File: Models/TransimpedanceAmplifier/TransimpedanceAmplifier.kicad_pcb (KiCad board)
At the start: 2 copper layers, 107 parts, among them J1 Conn_01x02_Socket, J10 Conn_01x02_Pin, J11 Conn_01x24_Socket, J14 Conn_01x24_Socket, J2 Conn_01x02_Socket, J3 Conn_01x03_Pin, J4 Conn_01x02_Pin, J5 Conn_01x02_Pin, J6 Conn_01x02_Pin, J7 Conn_01x02_Pin, J8 Conn_01x02_Pin, J9 Conn_01x02_Pin, Q1 Q_PNP, Q2 Q_NPN, U1 LM7905, -5V, 5%, U10 DAC81401, U11 ISO7641FM, U12 ISO7641FM, U13 ADS8699, U2 LM7805, 5V, 5%, U3 OPA828, U4 AD8615, U5 OP37GPZ, U6 LM7915, -15V, 5%, U7 LM7815, 15V, 5%, U8 LM7805, 5V, 5%, U9 TLV76133, 3.3V, 1%

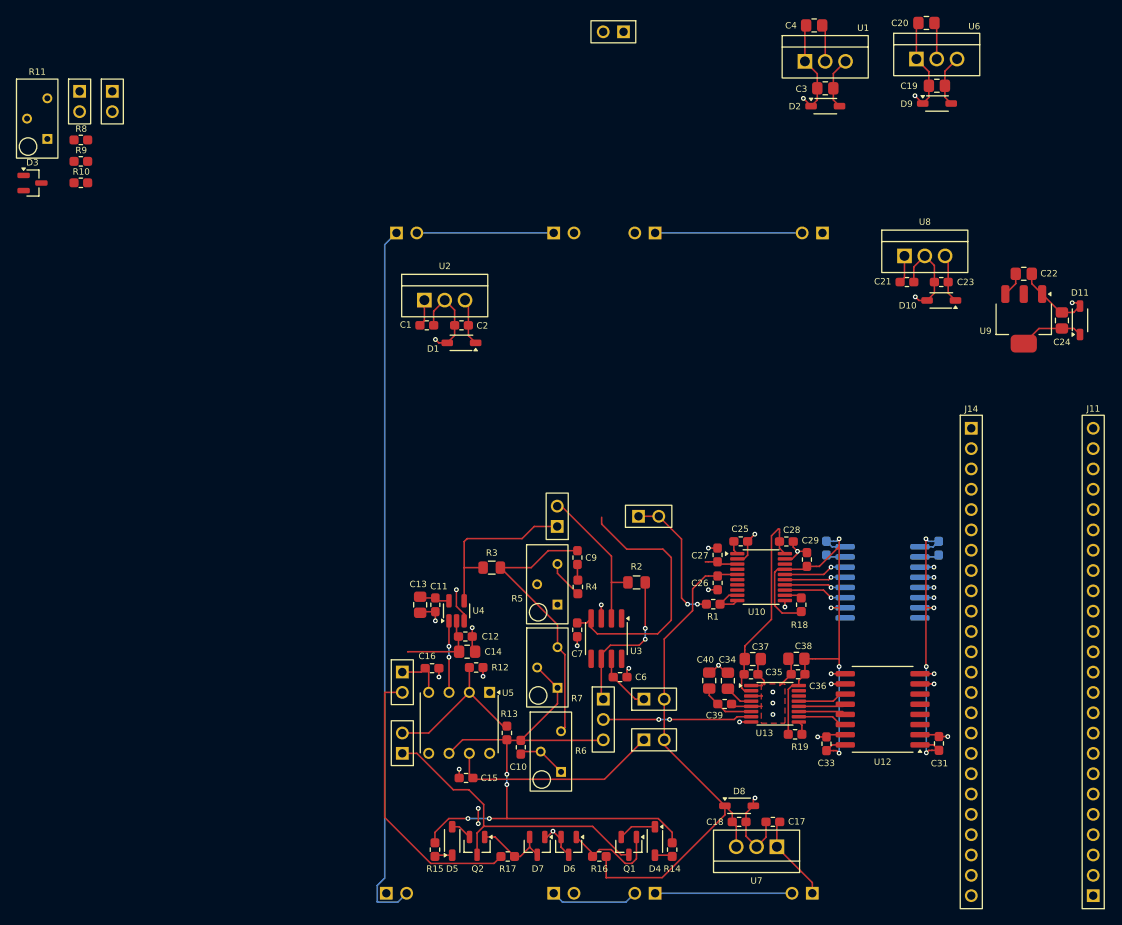
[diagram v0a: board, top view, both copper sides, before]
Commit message: Aligned the voltage regulators
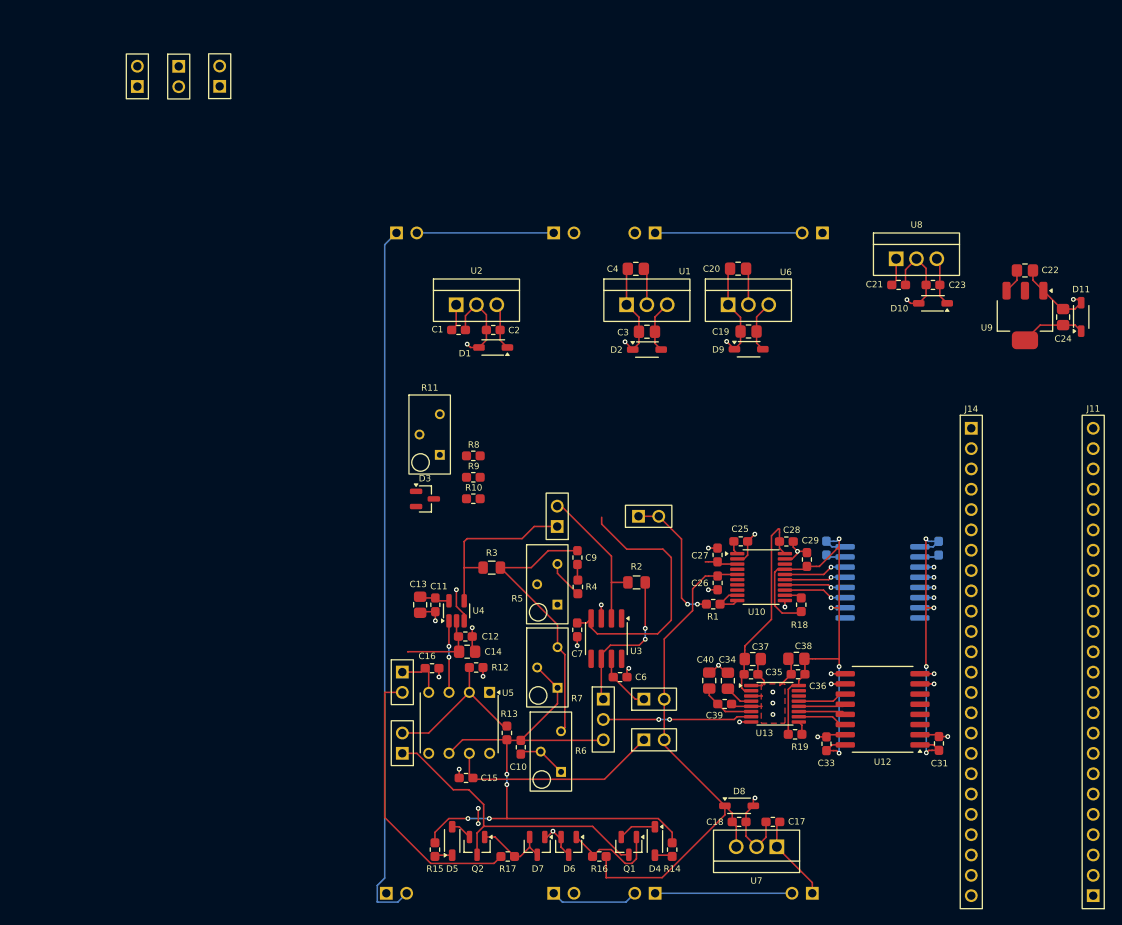
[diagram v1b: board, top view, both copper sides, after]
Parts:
- moved R10 63.0 mm to (87.0, 83.5)
- moved R8 63.0 mm to (87.0, 78.1)
- moved D3 63.0 mm to (81.0, 83.5)
- moved R11 63.0 mm to (81.6, 75.4)
- moved R9 63.0 mm to (87.0, 80.8)
- moved J5 49.5 mm to (55.3, 30.6), turned to 180 degrees
- moved C19 38.7 mm to (121.4, 62.6)
- moved C20 38.7 mm to (120.1, 54.7)
- moved D9 38.7 mm to (121.4, 64.8)
- moved U6 38.7 mm to (121.4, 59.2)
- moved C3 37.7 mm to (108.7, 62.6)
- moved C4 37.7 mm to (107.3, 54.7)
- moved U1 37.7 mm to (108.7, 59.2)
- moved D2 37.7 mm to (108.7, 64.8)
- moved J6 12.8 mm to (50.2, 30.7)
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
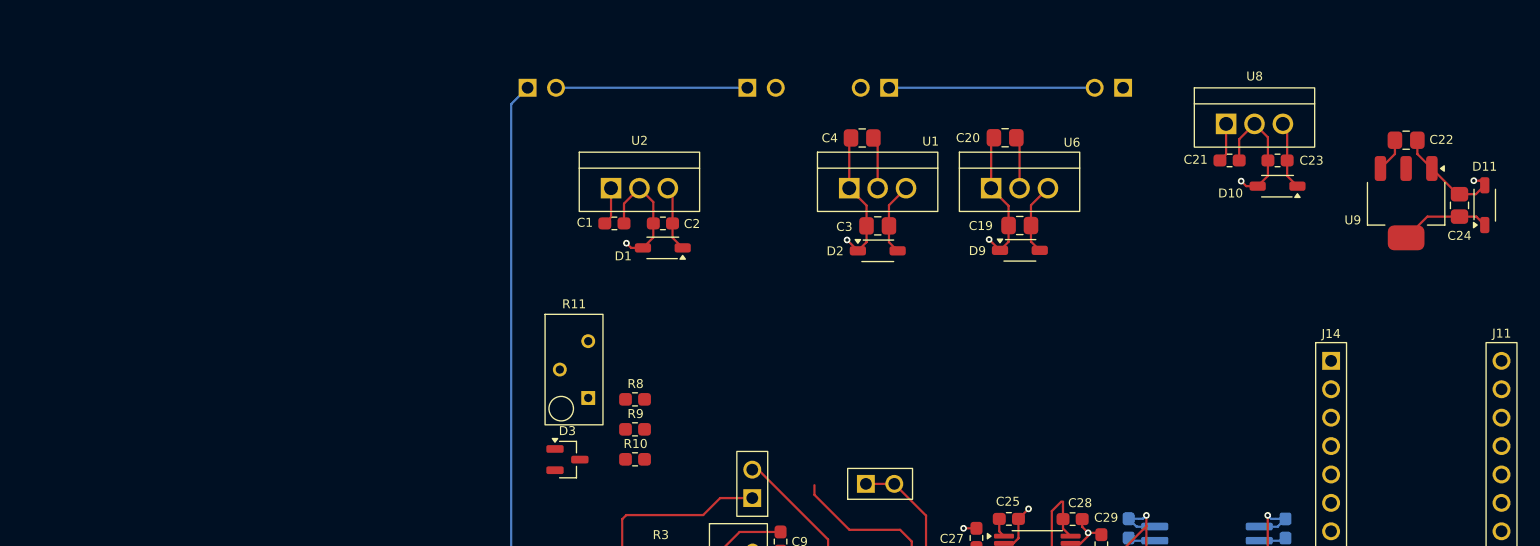
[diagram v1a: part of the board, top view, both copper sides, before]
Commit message: Next step is silkscreen labels for the voltages
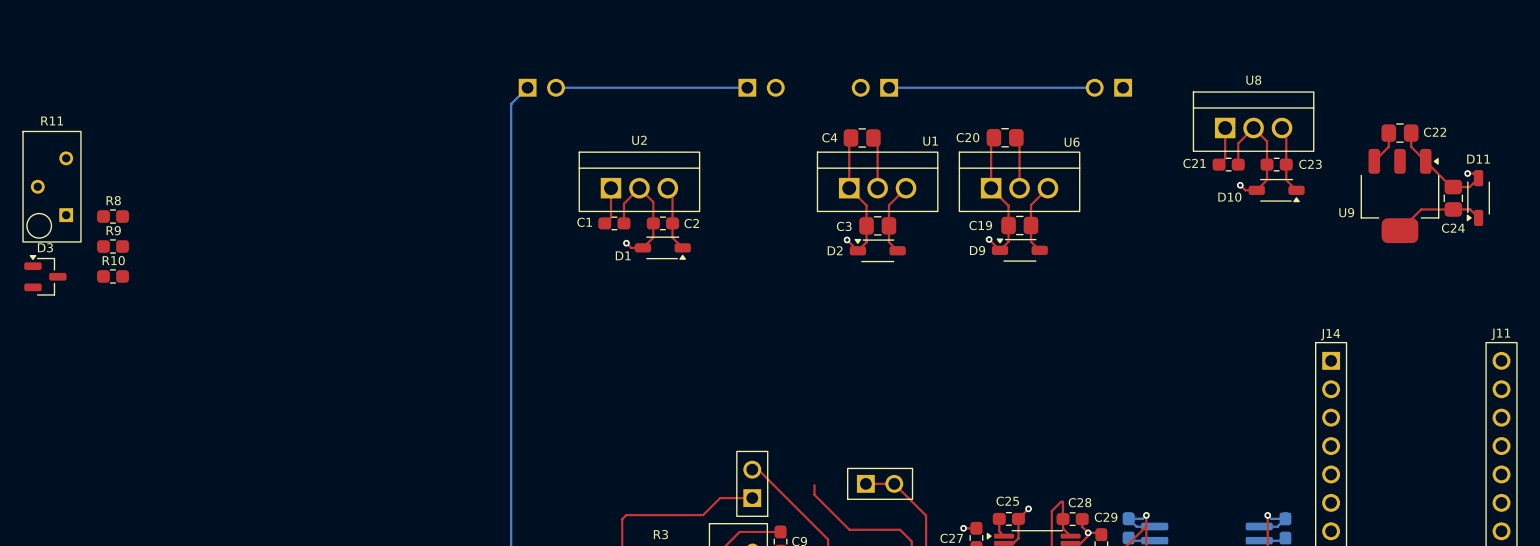
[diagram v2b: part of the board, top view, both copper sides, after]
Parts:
- moved R10 49.5 mm to (40.3, 67.1)
- moved D3 49.5 mm to (34.3, 67.1)
- moved R11 49.5 mm to (34.9, 59.1)
- moved R8 49.5 mm to (40.3, 61.8)
- moved R9 49.5 mm to (40.3, 64.4)
- moved C22 0.84 mm to (155.4, 54.3)
- moved C24 0.84 mm to (160.2, 60.1)
- moved D11 0.84 mm to (162.4, 60.1)
- moved U9 0.84 mm to (155.4, 59.9)
- moved U8 0.38 mm to (142.3, 53.8)
- moved C21 0.38 mm to (140.1, 57.1)
- moved C23 0.38 mm to (144.4, 57.1)
- moved D10 0.38 mm to (144.4, 59.4)
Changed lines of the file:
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@@
 	(footprint "TwoTerminal:CAPC0805"
 		(layer "F.Cu")
-		(at 160.74 60.76 90)
+		(at 160.19 60.12 90)
 		(property "Reference" "C24"
 			(at -2.71 0 0)
@@
 	)
 	(footprint "ThreeTerminal:TO-220"
+		(locked yes)
 		(layer "F.Cu")
-		(at 142.41 53.47)
+		(at 142.33 53.84)
 		(property "Reference" "U8"
 			(at 0.01 -4.25 0)
@@
 	)
 	(footprint "ThreeTerminal:TO-220"
+		(locked yes)
 		(layer "F.Cu")
 		(at 108.71 59.22)
@@
 	(footprint "ThreeTerminal:SOT-23"
 		(layer "F.Cu")
-		(at 80.97 83.49)
+		(at 34.29 67.14)
 		(property "Reference" "D3"
 			(at -0.005 -2.5625 0)
@@
 	(footprint "TwoTerminal:SOD-123"
 		(layer "F.Cu")
-		(at 144.47 59.04 180)
+		(at 144.39 59.41 180)
 		(property "Reference" "D10"
 			(at 4.2 -0.64 0)
@@
 	(footprint "TwoTerminal:RESC0603"
 		(layer "F.Cu")
-		(at 87.015 78.105)
+		(at 40.335 61.755)
 		(property "Reference" "R8"
 			(at 0.0475 -1.385 0)
@@
 	)
 	(footprint "ThreeTerminal:SOT-223"
+		(locked yes)
 		(layer "F.Cu")
-		(at 155.97 60.56 -90)
+		(at 155.42 59.92 -90)
 		(property "Reference" "U9"
 			(at 1.52 4.77 0)
@@
 	)
 	(footprint "ThreeTerminal:TO-220"
+		(locked yes)
 		(layer "F.Cu")
 		(at 121.4 59.22)
@@
 	(footprint "ThreeTerminal:Bourns_3296Y"
 		(layer "F.Cu")
-		(at 81.56 75.44)
+		(at 34.88 59.09)
 		(property "Reference" "R11"
 			(at 0.0075 -5.85 0)
@@
 	(footprint "TwoTerminal:CAPC0603"
 		(layer "F.Cu")
-		(at 144.47 56.74 180)
+		(at 144.39 57.11 180)
 		(property "Reference" "C23"
 			(at -3.04 -0.01 0)
@@
 	(footprint "TwoTerminal:CAPC0805"
 		(layer "F.Cu")
-		(at 155.97 54.93)
+		(at 155.42 54.29)
 		(property "Reference" "C22"
 			(at 3.16 -0.04 0)
@@
 	(footprint "TwoTerminal:RESC0603"
 		(layer "F.Cu")
-		(at 87.015 83.465)
+		(at 40.335 67.115)
 		(property "Reference" "R10"
 			(at 0.0475 -1.385 0)
@@
 	)
 	(footprint "ThreeTerminal:TO-220"
+		(locked yes)
 		(layer "F.Cu")
 		(at 87.41 59.22)
@@
 	(footprint "TwoTerminal:CAPC0603"
 		(layer "F.Cu")
-		(at 140.18 56.74)
+		(at 140.1 57.11)
 		(property "Reference" "C21"
 			(at -3.03 -0.07 0)
@@
 	(footprint "TwoTerminal:RESC0603"
 		(layer "F.Cu")
-		(at 87.015 80.785)
+		(at 40.335 64.435)
 		(property "Reference" "R9"
 			(at 0.0475 -1.385 0)
@@
 	(footprint "TwoTerminal:SOD-123"
 		(layer "F.Cu")
-		(at 163 60.74 90)
+		(at 162.45 60.1 90)
 		(property "Reference" "D11"
 			(at 3.45 -0.01 0)
@@
 	)
 	(gr_text "2.5 V"
-		(at 80.41 90.91 90)
+		(at 33.73 74.56 90)
 		(layer "User.2")
 		(effects
@@
 	)
 	(gr_text "3.3 V"
-		(at 148.79 64.72 0)
+		(at 148.24 64.08 0)
 		(layer "User.2")
 		(effects
@@
 	)
 	(gr_text "-1.5 V"
-		(at 78.63 91.88 90)
+		(at 31.95 75.53 90)
 		(layer "User.2")
 		(effects
@@
 	)
 	(gr_text "5 V"
-		(at 135.7975 59.41 0)
+		(at 135.7175 59.78 0)
 		(layer "User.2")
 		(effects
@@
 	)
 	(segment
-		(start 139.87 53.47)
-		(end 139.87 56.19)
+		(start 139.79 53.84)
+		(end 139.79 56.56)
 		(width 0.2)
 		(layer "F.Cu")
@@
 	)
 	(segment
-		(start 139.87 56.19)
-		(end 139.32 56.74)
+		(start 139.79 56.56)
+		(end 139.24 57.11)
 		(width 0.2)
 		(layer "F.Cu")
@@
 	)
 	(segment
-		(start 163 58.96)
-		(end 162.6 58.56)
+		(start 162.45 58.32)
+		(end 162.05 57.92)
 		(width 0.2)
 		(layer "F.Cu")
@@
 	)
 	(segment
-		(start 156.9725 54.93)
-		(end 156.9725 56.1625)
+		(start 156.4225 54.29)
+		(end 156.4225 55.5225)
 		(width 0.2)
 		(layer "F.Cu")
@@
 	)
 	(segment
-		(start 156.9725 56.1625)
-		(end 158.27 57.46)
+		(start 156.4225 55.5225)
+		(end 157.72 56.82)
 		(width 0.2)
 		(layer "F.Cu")
@@
 	)
 	(segment
-		(start 143.61 54.67)
-		(end 142.41 53.47)
+		(start 143.53 55.04)
+		(end 142.33 53.84)
 		(width 0.2)
 		(layer "F.Cu")
@@
 	)
 	(segment
-		(start 160.5675 59.7575)
-		(end 158.27 57.46)
+		(start 160.0175 59.1175)
+		(end 157.72 56.82)
 		(width 0.2)
 		(layer "F.Cu")
@@
 	)
 	(segment
-		(start 141.04 56.74)
-		(end 141.04 54.84)
+		(start 140.96 57.11)
+		(end 140.96 55.21)
 		(width 0.2)
 		(layer "F.Cu")
@@
 	)
 	(segment
-		(start 143.61 56.74)
-		(end 143.61 58.1225)
+		(start 143.53 57.11)
+		(end 143.53 58.4925)
 		(width 0.2)
 		(layer "F.Cu")
@@
 	)
 	(segment
-		(start 160.74 59.7575)
-		(end 162.205 59.7575)
+		(start 160.19 59.1175)
+		(end 161.655 59.1175)
 		(width 0.2)
 		(layer "F.Cu")
@@
 	)
 	(segment
-		(start 160.74 59.7575)
-		(end 160.5675 59.7575)
+		(start 160.19 59.1175)
+		(end 160.0175 59.1175)
 		(width 0.2)
 		(layer "F.Cu")
@@
 	)
 	(segment
-		(start 143.61 58.1225)
-		(end 142.6925 59.04)
+		(start 143.53 58.4925)
+		(end 142.6125 59.41)
 		(width 0.2)
 		(layer "F.Cu")
@@
 	)
 	(segment
-		(start 162.59 58.55)
-		(end 162.02 58.55)
+		(start 162.04 57.91)
+		(end 161.47 57.91)
 		(width 0.2)
 		(layer "F.Cu")
@@
 	)
 	(segment
-		(start 141.04 54.84)
-		(end 142.41 53.47)
+		(start 140.96 55.21)
+		(end 142.33 53.84)
 		(width 0.2)
 		(layer "F.Cu")
@@
 	)
 	(segment
-		(start 163 58.9625)
-		(end 163 58.96)
+		(start 162.45 58.3225)
+		(end 162.45 58.32)
 		(width 0.2)
 		(layer "F.Cu")
@@
 	)
 	(segment
-		(start 162.6 58.56)
-		(end 162.59 58.55)
+		(start 162.05 57.92)
+		(end 162.04 57.91)
 		(width 0.2)
 		(layer "F.Cu")
@@
 	)
 	(segment
-		(start 142.6925 59.04)
-		(end 141.67 59.04)
+		(start 142.6125 59.41)
+		(end 141.59 59.41)
 		(width 0.2)
 		(layer "F.Cu")
@@
 	)
 	(segment
-		(start 162.205 59.7575)
-		(end 163 58.9625)
+		(start 161.655 59.1175)
+		(end 162.45 58.3225)
 		(width 0.2)
 		(layer "F.Cu")
@@
 	)
 	(segment
-		(start 143.61 56.74)
-		(end 143.61 54.67)
+		(start 143.53 57.11)
+		(end 143.53 55.04)
 		(width 0.2)
 		(layer "F.Cu")
@@
 	)
 	(segment
-		(start 141.67 59.04)
-		(end 141.22 58.59)
+		(start 141.59 59.41)
+		(end 141.14 58.96)
 		(width 0.2)
 		(layer "F.Cu")
@@
 	)
 	(via
-		(at 141.22 58.59)
+		(at 141.14 58.96)
 		(size 0.6)
 		(drill 0.3)
@@
 	)
 	(via
-		(at 162.02 58.55)
+		(at 161.47 57.91)
 		(size 0.6)
 		(drill 0.3)
@@
 	)
 	(segment
-		(start 145.33 56.74)
-		(end 145.33 58.1225)
+		(start 145.25 57.11)
+		(end 145.25 58.4925)
 		(width 0.2)
 		(layer "F.Cu")
@@
 	)
 	(segment
-		(start 145.33 56.74)
-		(end 145.33 53.85)
+		(start 145.25 57.11)
+		(end 145.25 54.22)
 		(width 0.2)
 		(layer "F.Cu")
@@
 	)
 	(segment
-		(start 145.33 53.85)
-		(end 144.95 53.47)
+		(start 145.25 54.22)
+		(end 144.87 53.84)
 		(width 0.2)
 		(layer "F.Cu")
@@
 	)
 	(segment
-		(start 145.33 58.1225)
-		(end 146.2475 59.04)
+		(start 145.25 58.4925)
+		(end 146.1675 59.41)
 		(width 0.2)
 		(layer "F.Cu")
@@
 	)
 	(segment
-		(start 154.9675 54.93)
-		(end 154.9675 56.1625)
+		(start 154.4175 54.29)
+		(end 154.4175 55.5225)
 		(width 0.2)
 		(layer "F.Cu")
@@
 	)
 	(segment
-		(start 154.9675 56.1625)
-		(end 153.67 57.46)
+		(start 154.4175 55.5225)
+		(end 153.12 56.82)
 		(width 0.2)
 		(layer "F.Cu")
@@
 	)
 	(segment
-		(start 160.74 61.7625)
-		(end 162.245 61.7625)
+		(start 160.19 61.1225)
+		(end 161.695 61.1225)
 		(width 0.2)
 		(layer "F.Cu")
@@
 	)
 	(segment
-		(start 160.74 61.7625)
-		(end 157.8675 61.7625)
+		(start 160.19 61.1225)
+		(end 157.3175 61.1225)
 		(width 0.2)
 		(layer "F.Cu")
@@
 	)
 	(segment
-		(start 157.8675 61.7625)
-		(end 155.97 63.66)
+		(start 157.3175 61.1225)
+		(end 155.42 63.02)
 		(width 0.2)
 		(layer "F.Cu")
@@
 	)
 	(segment
-		(start 162.245 61.7625)
-		(end 163 62.5175)
+		(start 161.695 61.1225)
+		(end 162.45 61.8775)
 		(width 0.2)
 		(layer "F.Cu")
